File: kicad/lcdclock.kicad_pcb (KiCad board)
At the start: 2 copper layers, 41 x 50 mm, 28 parts, among them J1 Conn_JLink_SWD, Q1 BSH205, SW1 SW_Push, U1 STM32L073xx_48, U2 ELV_DCF-2, U3 TPS70630, U4 LCD, Y1 32.768kHz 12.5pF

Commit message: Unify drill sizes
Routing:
- net Net-(U1-Pad11): track 27.1 -> 27.8 mm
- net Net-(U1-Pad17): track 22.3 -> 22.8 mm
- net Net-(U1-Pad13): track 23.0 -> 23.5 mm

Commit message: Final fixes
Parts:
- BT1: value 4xAA 6.4-3.2V -> 4xAAA 6.4-3.2V
- R1: value 100k -> ?
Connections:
- J1 pad 11: (no net) -> Net-(J1-Pad11)
- J1 pad 13: (no net) -> Net-(J1-Pad13)
- J1 pad 17: (no net) -> Net-(J1-Pad17)
- J1 pad 19: (no net) -> Net-(J1-Pad19)
- J1 pad 2: (no net) -> Net-(J1-Pad2)
- J1 pad 3: (no net) -> Net-(J1-Pad3)
- J1 pad 5: (no net) -> Net-(J1-Pad5)
- U1 pad 25: (no net) -> Net-(U1-Pad25)
- U1 pad 26: (no net) -> Net-(U1-Pad26)
- U1 pad 27: (no net) -> Net-(U1-Pad27)
- U1 pad 28: (no net) -> Net-(U1-Pad28)
- U1 pad 38: (no net) -> Net-(U1-Pad38)
- U1 pad 44: (no net) -> GND
- U1 pad 45: (no net) -> Net-(U1-Pad45)
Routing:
- net GND: track 45.9 -> 48.1 mm
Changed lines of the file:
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@@
 (kicad_pcb (version 4) (host pcbnew 4.0.7)
   (general
-    (links 83)
+    (links 84)
     (no_connects 0)
     (area 19.924999 19.924999 61.075001 70.075001)
     (thickness 1.6)
     (drawings 5)
-    (tracks 375)
+    (tracks 377)
     (zones 0)
     (modules 28)
-    (nets 32)
+    (nets 45)
   )
   (page A4)
@@
   (net 30 "Net-(C14-Pad1)")
   (net 31 "Net-(Q1-Pad1)")
+  (net 32 "Net-(J1-Pad2)")
+  (net 33 "Net-(J1-Pad3)")
+  (net 34 "Net-(J1-Pad5)")
+  (net 35 "Net-(J1-Pad11)")
+  (net 36 "Net-(J1-Pad13)")
+  (net 37 "Net-(J1-Pad17)")
+  (net 38 "Net-(J1-Pad19)")
+  (net 39 "Net-(U1-Pad25)")
+  (net 40 "Net-(U1-Pad26)")
+  (net 41 "Net-(U1-Pad27)")
+  (net 42 "Net-(U1-Pad28)")
+  (net 43 "Net-(U1-Pad38)")
+  (net 44 "Net-(U1-Pad45)")
   (net_class Default "This is the default net class."
     (clearance 0.2)
@@
     (add_net "Net-(C5-Pad2)")
     (add_net "Net-(D1-Pad2)")
+    (add_net "Net-(J1-Pad11)")
+    (add_net "Net-(J1-Pad13)")
+    (add_net "Net-(J1-Pad17)")
+    (add_net "Net-(J1-Pad19)")
+    (add_net "Net-(J1-Pad2)")
+    (add_net "Net-(J1-Pad3)")
+    (add_net "Net-(J1-Pad5)")
     (add_net "Net-(J1-Pad7)")
     (add_net "Net-(J1-Pad9)")
@@
     (add_net "Net-(U1-Pad21)")
     (add_net "Net-(U1-Pad22)")
+    (add_net "Net-(U1-Pad25)")
+    (add_net "Net-(U1-Pad26)")
+    (add_net "Net-(U1-Pad27)")
+    (add_net "Net-(U1-Pad28)")
     (add_net "Net-(U1-Pad29)")
     (add_net "Net-(U1-Pad30)")
     (add_net "Net-(U1-Pad31)")
+    (add_net "Net-(U1-Pad38)")
     (add_net "Net-(U1-Pad39)")
     (add_net "Net-(U1-Pad40)")
     (add_net "Net-(U1-Pad41)")
     (add_net "Net-(U1-Pad43)")
+    (add_net "Net-(U1-Pad45)")
     (add_net "Net-(U1-Pad46)")
     (add_net VCC)
@@
     (pad 1 thru_hole rect (at 0 0 90) (size 1.7272 1.7272) (drill 1.016) (layers *.Cu *.Mask)
       (net 5 VCC))
-    (pad 2 thru_hole oval (at 0 -2.54 90) (size 1.7272 1.7272) (drill 1.016) (layers *.Cu *.Mask))
-    (pad 3 thru_hole oval (at 2.54 0 90) (size 1.7272 1.7272) (drill 1.016) (layers *.Cu *.Mask))
+    (pad 2 thru_hole oval (at 0 -2.54 90) (size 1.7272 1.7272) (drill 1.016) (layers *.Cu *.Mask)
+      (net 32 "Net-(J1-Pad2)"))
+    (pad 3 thru_hole oval (at 2.54 0 90) (size 1.7272 1.7272) (drill 1.016) (layers *.Cu *.Mask)
+      (net 33 "Net-(J1-Pad3)"))
     (pad 4 thru_hole oval (at 2.54 -2.54 90) (size 1.7272 1.7272) (drill 1.016) (layers *.Cu *.Mask)
       (net 2 GND))
-    (pad 5 thru_hole oval (at 5.08 0 90) (size 1.7272 1.7272) (drill 1.016) (layers *.Cu *.Mask))
+    (pad 5 thru_hole oval (at 5.08 0 90) (size 1.7272 1.7272) (drill 1.016) (layers *.Cu *.Mask)
+      (net 34 "Net-(J1-Pad5)"))
     (pad 6 thru_hole oval (at 5.08 -2.54 90) (size 1.7272 1.7272) (drill 1.016) (layers *.Cu *.Mask)
       (net 2 GND))
@@
     (pad 10 thru_hole oval (at 10.16 -2.54 90) (size 1.7272 1.7272) (drill 1.016) (layers *.Cu *.Mask)
       (net 2 GND))
-    (pad 11 thru_hole oval (at 12.7 0 90) (size 1.7272 1.7272) (drill 1.016) (layers *.Cu *.Mask))
+    (pad 11 thru_hole oval (at 12.7 0 90) (size 1.7272 1.7272) (drill 1.016) (layers *.Cu *.Mask)
+      (net 35 "Net-(J1-Pad11)"))
     (pad 12 thru_hole oval (at 12.7 -2.54 90) (size 1.7272 1.7272) (drill 1.016) (layers *.Cu *.Mask)
       (net 2 GND))
-    (pad 13 thru_hole oval (at 15.24 0 90) (size 1.7272 1.7272) (drill 1.016) (layers *.Cu *.Mask))
+    (pad 13 thru_hole oval (at 15.24 0 90) (size 1.7272 1.7272) (drill 1.016) (layers *.Cu *.Mask)
+      (net 36 "Net-(J1-Pad13)"))
     (pad 14 thru_hole oval (at 15.24 -2.54 90) (size 1.7272 1.7272) (drill 1.016) (layers *.Cu *.Mask)
       (net 2 GND))
@@
     (pad 16 thru_hole oval (at 17.78 -2.54 90) (size 1.7272 1.7272) (drill 1.016) (layers *.Cu *.Mask)
       (net 2 GND))
-    (pad 17 thru_hole oval (at 20.32 0 90) (size 1.7272 1.7272) (drill 1.016) (layers *.Cu *.Mask))
+    (pad 17 thru_hole oval (at 20.32 0 90) (size 1.7272 1.7272) (drill 1.016) (layers *.Cu *.Mask)
+      (net 37 "Net-(J1-Pad17)"))
     (pad 18 thru_hole oval (at 20.32 -2.54 90) (size 1.7272 1.7272) (drill 1.016) (layers *.Cu *.Mask)
       (net 2 GND))
-    (pad 19 thru_hole oval (at 22.86 0 90) (size 1.7272 1.7272) (drill 1.016) (layers *.Cu *.Mask))
+    (pad 19 thru_hole oval (at 22.86 0 90) (size 1.7272 1.7272) (drill 1.016) (layers *.Cu *.Mask)
+      (net 38 "Net-(J1-Pad19)"))
     (pad 20 thru_hole oval (at 22.86 -2.54 90) (size 1.7272 1.7272) (drill 1.016) (layers *.Cu *.Mask)
       (net 2 GND))
@@
       (effects (font (size 1 1) (thickness 0.15)))
     )
-    (fp_text value 100k (at 0 1.75 90) (layer F.Fab)
+    (fp_text value ? (at 0 1.75 90) (layer F.Fab)
       (effects (font (size 1 1) (thickness 0.15)))
     )
@@
     (pad 24 smd rect (at 2.75 4.35 90) (size 1.3 0.25) (layers F.Cu F.Paste F.Mask)
       (net 5 VCC))
-    (pad 25 smd rect (at 4.35 2.75) (size 1.3 0.25) (layers F.Cu F.Paste F.Mask))
-    (pad 26 smd rect (at 4.35 2.25) (size 1.3 0.25) (layers F.Cu F.Paste F.Mask))
-    (pad 27 smd rect (at 4.35 1.75) (size 1.3 0.25) (layers F.Cu F.Paste F.Mask))
-    (pad 28 smd rect (at 4.35 1.25) (size 1.3 0.25) (layers F.Cu F.Paste F.Mask))
+    (pad 25 smd rect (at 4.35 2.75) (size 1.3 0.25) (layers F.Cu F.Paste F.Mask)
+      (net 39 "Net-(U1-Pad25)"))
+    (pad 26 smd rect (at 4.35 2.25) (size 1.3 0.25) (layers F.Cu F.Paste F.Mask)
+      (net 40 "Net-(U1-Pad26)"))
+    (pad 27 smd rect (at 4.35 1.75) (size 1.3 0.25) (layers F.Cu F.Paste F.Mask)
+      (net 41 "Net-(U1-Pad27)"))
+    (pad 28 smd rect (at 4.35 1.25) (size 1.3 0.25) (layers F.Cu F.Paste F.Mask)
+      (net 42 "Net-(U1-Pad28)"))
     (pad 29 smd rect (at 4.35 0.75) (size 1.3 0.25) (layers F.Cu F.Paste F.Mask)
       (net 22 "Net-(U1-Pad29)"))
@@
     (pad 37 smd rect (at 2.75 -4.35 90) (size 1.3 0.25) (layers F.Cu F.Paste F.Mask)
       (net 11 "Net-(J1-Pad9)"))
-    (pad 38 smd rect (at 2.25 -4.35 90) (size 1.3 0.25) (layers F.Cu F.Paste F.Mask))
+    (pad 38 smd rect (at 2.25 -4.35 90) (size 1.3 0.25) (layers F.Cu F.Paste F.Mask)
+      (net 43 "Net-(U1-Pad38)"))
     (pad 39 smd rect (at 1.75 -4.35 90) (size 1.3 0.25) (layers F.Cu F.Paste F.Mask)
       (net 25 "Net-(U1-Pad39)"))
@@
     (pad 43 smd rect (at -0.25 -4.35 90) (size 1.3 0.25) (layers F.Cu F.Paste F.Mask)
       (net 29 "Net-(U1-Pad43)"))
-    (pad 44 smd rect (at -0.75 -4.35 90) (size 1.3 0.25) (layers F.Cu F.Paste F.Mask))
-    (pad 45 smd rect (at -1.25 -4.35 90) (size 1.3 0.25) (layers F.Cu F.Paste F.Mask))
+    (pad 44 smd rect (at -0.75 -4.35 90) (size 1.3 0.25) (layers F.Cu F.Paste F.Mask)
+      (net 2 GND))
+    (pad 45 smd rect (at -1.25 -4.35 90) (size 1.3 0.25) (layers F.Cu F.Paste F.Mask)
+      (net 44 "Net-(U1-Pad45)"))
     (pad 46 smd rect (at -1.75 -4.35 90) (size 1.3 0.25) (layers F.Cu F.Paste F.Mask)
       (net 28 "Net-(U1-Pad46)"))
@@
       (effects (font (size 1 1) (thickness 0.15)))
     )
-    (fp_text value "4xAA 6.4-3.2V" (at 1.905 -4.445 270) (layer F.Fab)
+    (fp_text value "4xAAA 6.4-3.2V" (at 1.905 -4.445 270) (layer F.Fab)
       (effects (font (size 1 1) (thickness 0.15)))
     )
@@
   (segment (start 52.25 23.15) (end 52.25 22.5) (width 0.25) (layer F.Cu) (net 1))
   (segment (start 46.75 27.5) (end 46.75 26.75) (width 0.25) (layer F.Cu) (net 1))
+  (segment (start 35.25 37.15) (end 35.25 35.35) (width 0.25) (layer F.Cu) (net 2))
+  (segment (start 35.25 35.35) (end 35 35.1) (width 0.25) (layer F.Cu) (net 2))
   (segment (start 43.9 21.75) (end 45.25 21.75) (width 0.25) (layer F.Cu) (net 2))
   (via (at 45.25 21.75) (size 0.6) (drill 0.4) (layers F.Cu B.Cu) (net 2))

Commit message: Final fixes
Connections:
- C7 pad 1: VCC -> Net-(C7-Pad1)
- U1 pad 1: VCC -> Net-(C7-Pad1)
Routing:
- net VCC: track 138.4 -> 117.2 mm
- net Net-(C7-Pad1): track 0.00 -> 2.87 mm
- net GND: track 48.1 -> 48.0 mm, vias 17 -> 18
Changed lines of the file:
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@@
 (kicad_pcb (version 4) (host pcbnew 4.0.7)
   (general
-    (links 84)
+    (links 83)
     (no_connects 0)
     (area 19.924999 19.924999 61.075001 70.075001)
     (thickness 1.6)
     (drawings 5)
-    (tracks 377)
+    (tracks 372)
     (zones 0)
     (modules 28)
-    (nets 45)
+    (nets 46)
   )
   (page A4)
@@
   (net 43 "Net-(U1-Pad38)")
   (net 44 "Net-(U1-Pad45)")
+  (net 45 "Net-(C7-Pad1)")
   (net_class Default "This is the default net class."
     (clearance 0.2)
@@
     (add_net "Net-(C14-Pad1)")
     (add_net "Net-(C5-Pad2)")
+    (add_net "Net-(C7-Pad1)")
     (add_net "Net-(D1-Pad2)")
     (add_net "Net-(J1-Pad11)")
@@
     (fp_line (start 2.35 0.9) (end -2.35 0.9) (layer F.CrtYd) (width 0.05))
     (pad 1 smd rect (at -1.35 0 90) (size 1.5 1.3) (layers F.Cu F.Paste F.Mask)
-      (net 5 VCC))
+      (net 45 "Net-(C7-Pad1)"))
     (pad 2 smd rect (at 1.35 0 90) (size 1.5 1.3) (layers F.Cu F.Paste F.Mask)
       (net 2 GND))
@@
     (fp_line (start -3.625 -3.175) (end -5 -3.175) (layer F.SilkS) (width 0.15))
     (pad 1 smd rect (at -4.35 -2.75) (size 1.3 0.25) (layers F.Cu F.Paste F.Mask)
-      (net 5 VCC))
+      (net 45 "Net-(C7-Pad1)"))
     (pad 2 smd rect (at -4.35 -2.25) (size 1.3 0.25) (layers F.Cu F.Paste F.Mask))
     (pad 3 smd rect (at -4.35 -1.75) (size 1.3 0.25) (layers F.Cu F.Paste F.Mask)
@@
   (segment (start 52.25 23.15) (end 52.25 22.5) (width 0.25) (layer F.Cu) (net 1))
   (segment (start 46.75 27.5) (end 46.75 26.75) (width 0.25) (layer F.Cu) (net 1))
-  (segment (start 35.25 37.15) (end 35.25 35.35) (width 0.25) (layer F.Cu) (net 2))
+  (segment (start 35.25 37.15) (end 35.25 38.5) (width 0.25) (layer F.Cu) (net 2))
+  (segment (start 35.25 38.5) (end 35 38.75) (width 0.25) (layer F.Cu) (net 2))
+  (via (at 35 38.75) (size 0.6) (drill 0.4) (layers F.Cu B.Cu) (net 2))
   (segment (start 35.25 35.35) (end 35 35.1) (width 0.25) (layer F.Cu) (net 2))
   (segment (start 43.9 21.75) (end 45.25 21.75) (width 0.25) (layer F.Cu) (net 2))
@@
   (segment (start 44.5 34) (end 44 33.5) (width 0.25) (layer F.Cu) (net 5))
   (segment (start 48.65 34) (end 45 34) (width 0.25) (layer F.Cu) (net 5))
-  (segment (start 42.25 31.75) (end 44.5 34) (width 0.25) (layer F.Cu) (net 5))
   (segment (start 44.5 34) (end 45 34) (width 0.25) (layer F.Cu) (net 5))
   (segment (start 49 35.35) (end 49 34.35) (width 0.25) (layer F.Cu) (net 5))
@@
   (via (at 42.25 44.4) (size 0.6) (drill 0.4) (layers F.Cu B.Cu) (net 5))
   (segment (start 41.85 33.5) (end 41.95 33.5) (width 0.25) (layer F.Cu) (net 5))
-  (segment (start 30.75 36.35) (end 30.75 36.25) (width 0.25) (layer F.Cu) (net 5))
-  (segment (start 32.5 34.5) (end 32.5 32.5) (width 0.25) (layer F.Cu) (net 5))
-  (segment (start 30.75 36.25) (end 32.5 34.5) (width 0.25) (layer F.Cu) (net 5))
-  (segment (start 32.5 32.5) (end 34 31) (width 0.25) (layer F.Cu) (net 5))
-  (segment (start 37.5 31.75) (end 42.25 31.75) (width 0.25) (layer F.Cu) (net 5))
   (segment (start 49 35.45) (end 49 35.35) (width 0.25) (layer F.Cu) (net 5))
-  (segment (start 34 31) (end 36.75 31) (width 0.25) (layer F.Cu) (net 5))
-  (segment (start 36.75 31) (end 37.5 31.75) (width 0.25) (layer F.Cu) (net 5))
   (segment (start 35 32.4) (end 41.65 32.4) (width 0.25) (layer F.Cu) (net 5))
   (segment (start 41.85 32.6) (end 41.85 33.5) (width 0.25) (layer F.Cu) (net 5))
@@
   (segment (start 33.25 33.25) (end 34.1 32.4) (width 0.25) (layer F.Cu) (net 5))
   (segment (start 34.1 32.4) (end 35 32.4) (width 0.25) (layer F.Cu) (net 5))
-  (segment (start 31.65 38.75) (end 31.65 37.25) (width 0.25) (layer F.Cu) (net 5))
-  (segment (start 31.65 37.25) (end 30.75 36.35) (width 0.25) (layer F.Cu) (net 5))
   (segment (start 29.25 44.35) (end 29.25 46.4) (width 0.25) (layer F.Cu) (net 5))
   (segment (start 29.70001 44.5364) (end 29.568205 44.668205) (width 0.25) (layer F.Cu) (net 5))
@@
   (segment (start 49.25 21.55) (end 46.8 21.55) (width 0.25) (layer F.Cu) (net 31))
   (segment (start 46.8 21.55) (end 46.6 21.75) (width 0.25) (layer F.Cu) (net 31))
+  (segment (start 30.75 36.35) (end 30.75 36.25) (width 0.25) (layer F.Cu) (net 45))
+  (segment (start 31.65 38.75) (end 31.65 37.25) (width 0.25) (layer F.Cu) (net 45))
+  (segment (start 31.65 37.25) (end 30.75 36.35) (width 0.25) (layer F.Cu) (net 45))
   (zone (net 2) (net_name GND) (layer B.Cu) (hatch edge 0.508)
     (connect_pads (clearance 0.508))

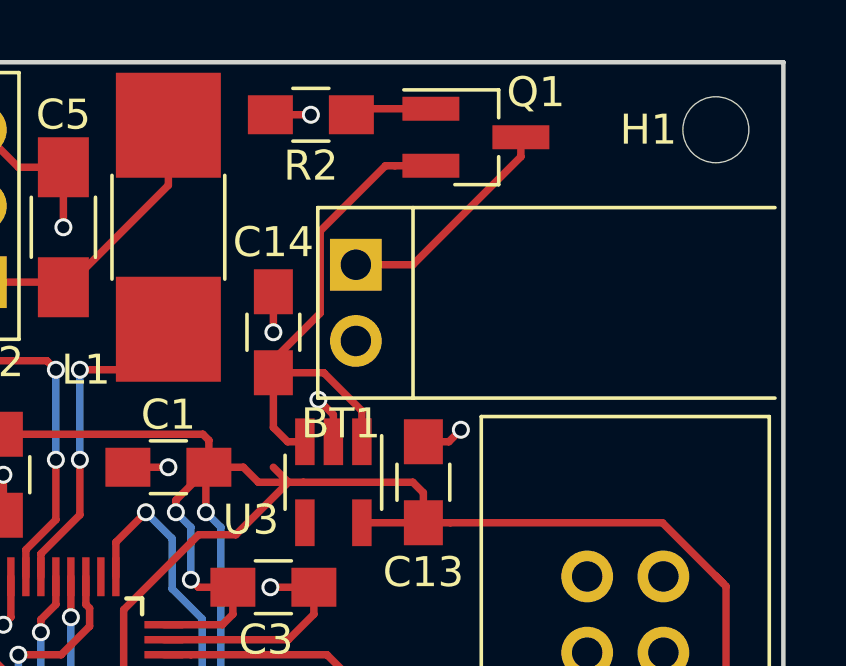
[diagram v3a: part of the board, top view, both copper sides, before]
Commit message: Fix two small issues in the PCB
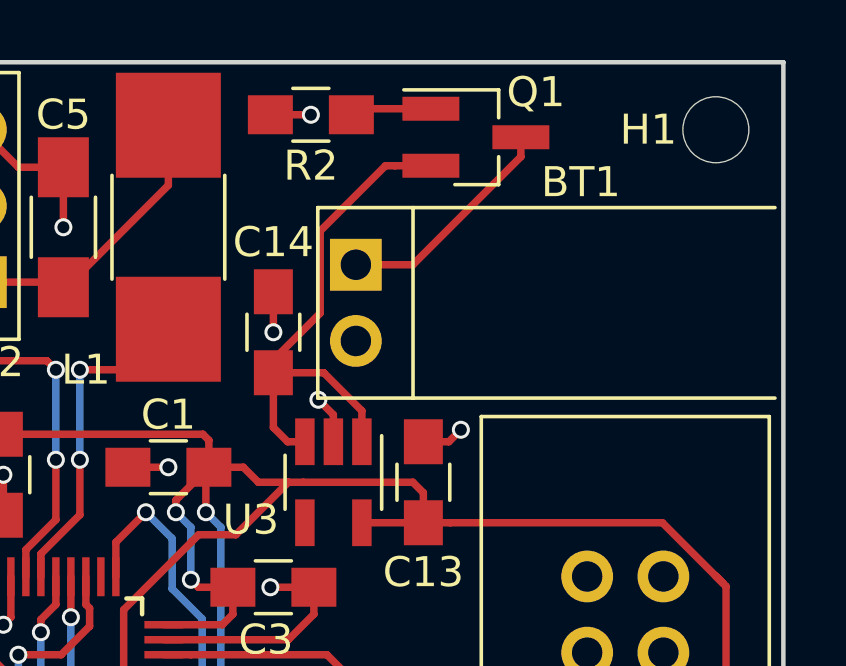
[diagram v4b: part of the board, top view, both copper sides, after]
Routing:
- net VCC: track 117.2 -> 116.5 mm
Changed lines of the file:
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@@
     (links 83)
     (no_connects 0)
-    (area 19.924999 19.924999 61.075001 70.075001)
+    (area 19.025 19.025 68.307143 72.025)
     (thickness 1.6)
     (drawings 5)
-    (tracks 372)
+    (tracks 371)
     (zones 0)
     (modules 28)
@@
       (padsonsilk false)
       (subtractmaskfromsilk false)
-      (outputformat 1)
+      (outputformat 2)
       (mirror false)
-      (drillshape 1)
+      (drillshape 0)
       (scaleselection 1)
-      (outputdirectory ""))
+      (outputdirectory C:/Users/michael/Desktop/))
   )
   (net 0 "")
@@
   (module "LCD Clock:CONNECTOR_2x1" (layer F.Cu)
     (at 46.75 26.75 270)
-    (fp_text reference BT1 (at 5.29 0.5 360) (layer F.SilkS)
+    (fp_text reference BT1 (at -2.75 -7.5 360) (layer F.SilkS)
       (effects (font (size 1 1) (thickness 0.15)))
     )
@@
   (segment (start 56.96913 35.35) (end 49.9 35.35) (width 0.25) (layer F.Cu) (net 5))
   (segment (start 49.9 35.35) (end 49 35.35) (width 0.25) (layer F.Cu) (net 5))
-  (segment (start 44.5 34) (end 44 33.5) (width 0.25) (layer F.Cu) (net 5))
   (segment (start 48.65 34) (end 45 34) (width 0.25) (layer F.Cu) (net 5))
   (segment (start 44.5 34) (end 45 34) (width 0.25) (layer F.Cu) (net 5))
